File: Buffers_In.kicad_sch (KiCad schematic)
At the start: 31 parts, among them U4 NE5532, U5 NE5532, X1 PEDAL_COMBO_TOP

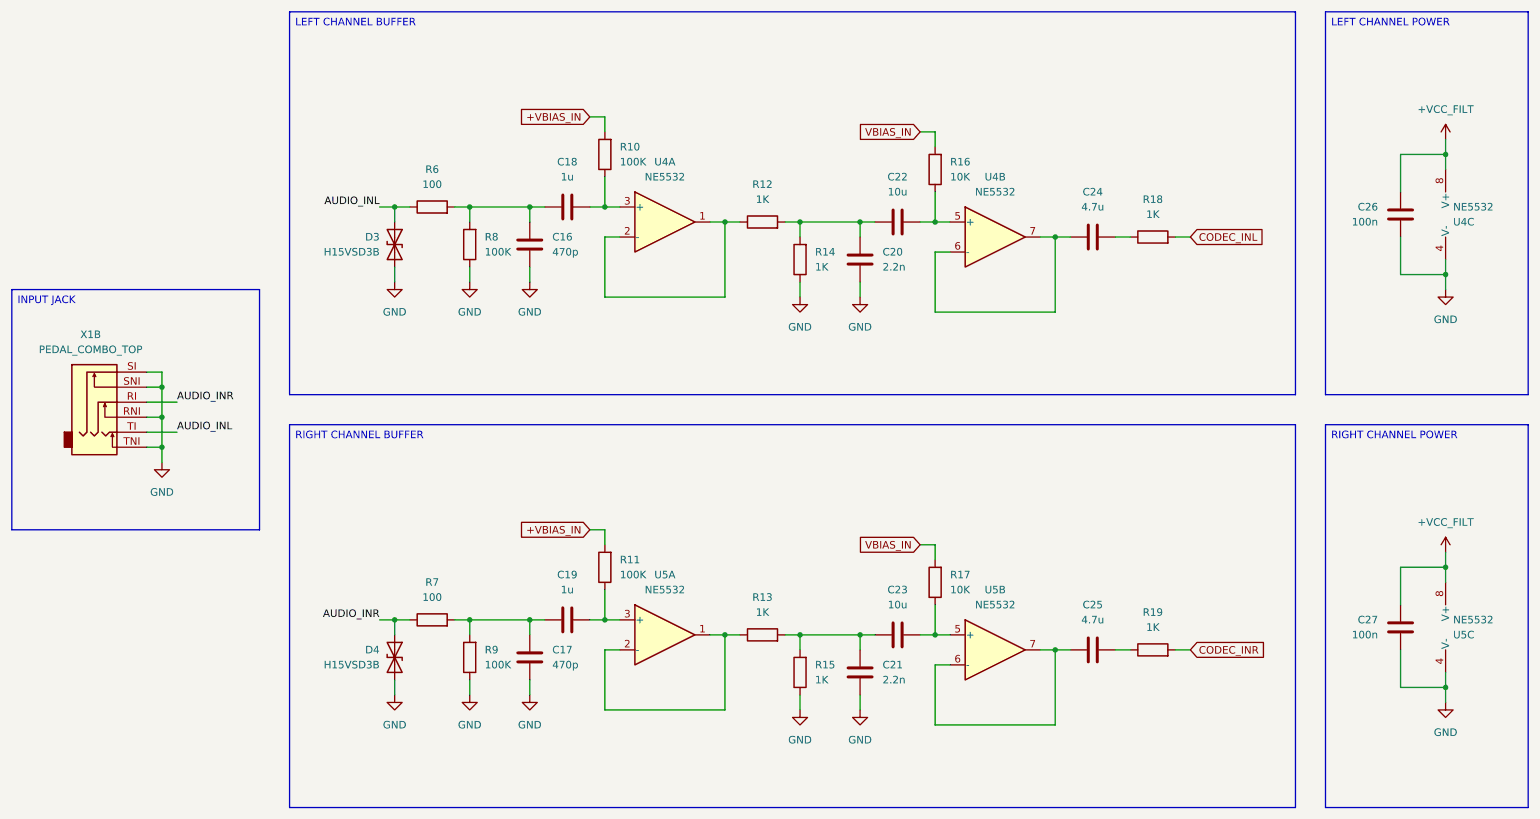
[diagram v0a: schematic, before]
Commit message: Buffer and layout
Updated the input and output buffers.
Updated the board layout.
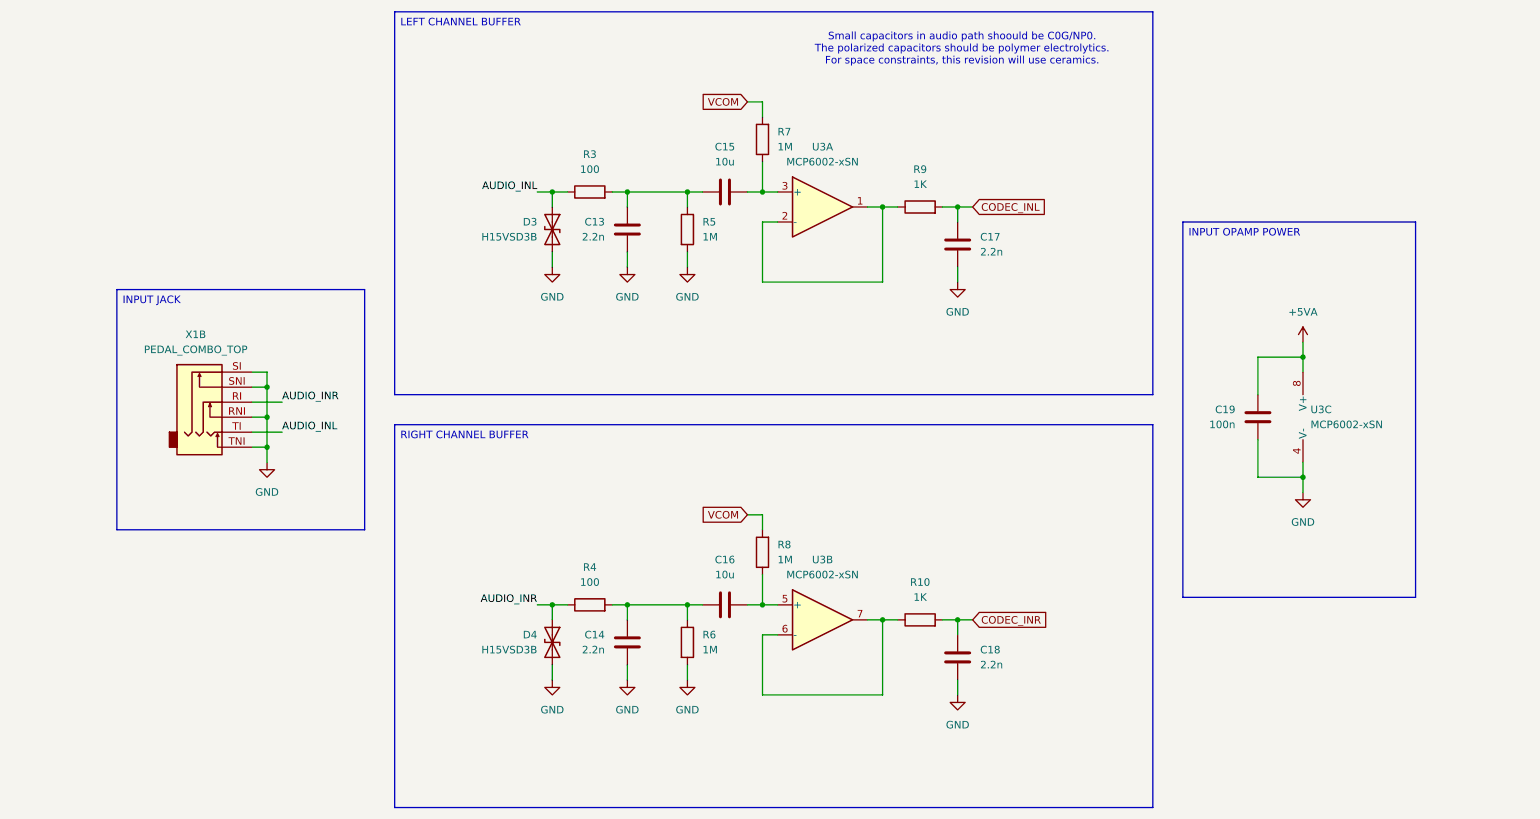
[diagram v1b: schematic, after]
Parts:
- removed C17: 470p, Capacitor_SMD:C_0603_1608Metric, symbol Device:C
- removed C19: 1u, Capacitor_SMD:C_0805_2012Metric, symbol Device:C
- removed C21: 2.2n, Capacitor_SMD:C_0603_1608Metric, symbol Device:C
- removed C22, C23: 10u, Capacitor_SMD:C_1206_3216Metric, symbol Device:C
- removed C24, C25: 4.7u, Capacitor_SMD:C_1206_3216Metric, symbol Device:C
- removed C27: 100n, Capacitor_SMD:C_0603_1608Metric, symbol Device:C
- removed R11, R9: 100K, Resistor_SMD:R_0603_1608Metric, symbol Device:R
- removed R13, R14, R15, R18, R19: 1K, Resistor_SMD:R_0603_1608Metric, symbol Device:R
- removed R16, R17: 10K, Resistor_SMD:R_0603_1608Metric, symbol Device:R
- removed R7: 100, Resistor_SMD:R_0603_1608Metric, symbol Device:R
- removed U4, U5: NE5532, Package_SO:SOIC-8_3.9x4.9mm_P1.27mm, symbol Amplifier_Operational:NE5532
- added C14: 2.2n, Capacitor_SMD:C_0805_2012Metric, symbol Device:C
- added C15, C16: 10u, Capacitor_SMD:C_1206_3216Metric, symbol Device:C
- added R10: 1K, Resistor_SMD:R_0603_1608Metric, symbol Device:R
- added R4: 100, Resistor_SMD:R_0603_1608Metric, symbol Device:R
- added R6, R8: 1M, Resistor_SMD:R_0603_1608Metric, symbol Device:R
- added U3: MCP6002-xSN, Package_SO:SOIC-8_3.9x4.9mm_P1.27mm, symbol Amplifier_Operational:MCP6002-xSN
- C13: renamed from C16; value 470p -> 2.2n; footprint Capacitor_SMD:C_0603_1608Metric -> Capacitor_SMD:C_0805_2012Metric
- C17: renamed from C20; footprint Capacitor_SMD:C_0603_1608Metric -> Capacitor_SMD:C_0805_2012Metric
- C18: value 1u -> 2.2n
- R5: renamed from R8; value 100K -> 1M
- R7: renamed from R10; value 100K -> 1M
- renumbered C26 to C19, R6 to R3, R12 to R9
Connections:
- net AUDIO_INR: now also R4.1
- net CODEC_INL: now also C17.1, R9.2
- net CODEC_INR: now also C18.1, R10.2
- net GND: now also C13.1, C18.2, R5.2, C14.1, R6.2, U3.4 (V-); no longer C13.2, R5.1
- net at R9.1: now also U3.1, U3.2 (-)
- net at R7.1: now also C15.2, U3.3 (+); no longer C18.2
- net +VBIAS_IN renamed VCOM
- net VCOM: now also R8.2
- net +VCC_FILT renamed +5VA
- net +5VA: now also U3.8 (V+)
- new net: C14.2, C16.1, R4.2, R6.1
- new net: R10.1, U3.6 (-), U3.7
- new net: C13.2, C15.1, R3.2, R5.1
- new net: C16.2, R8.1, U3.5 (+)
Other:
- note added: "Small capacitors in audio path shoould be C0G/NP0. The polarized capacitors should be polymer electrolytics. For space constraints, this revision will use ceramics."
- moved on the sheet: C13, C17, C19, D3, R3, R5, R7, R9, X1B
